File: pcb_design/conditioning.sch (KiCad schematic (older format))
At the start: 41 parts, among them U3 OPA2376AIDR, U4 LM2903DT

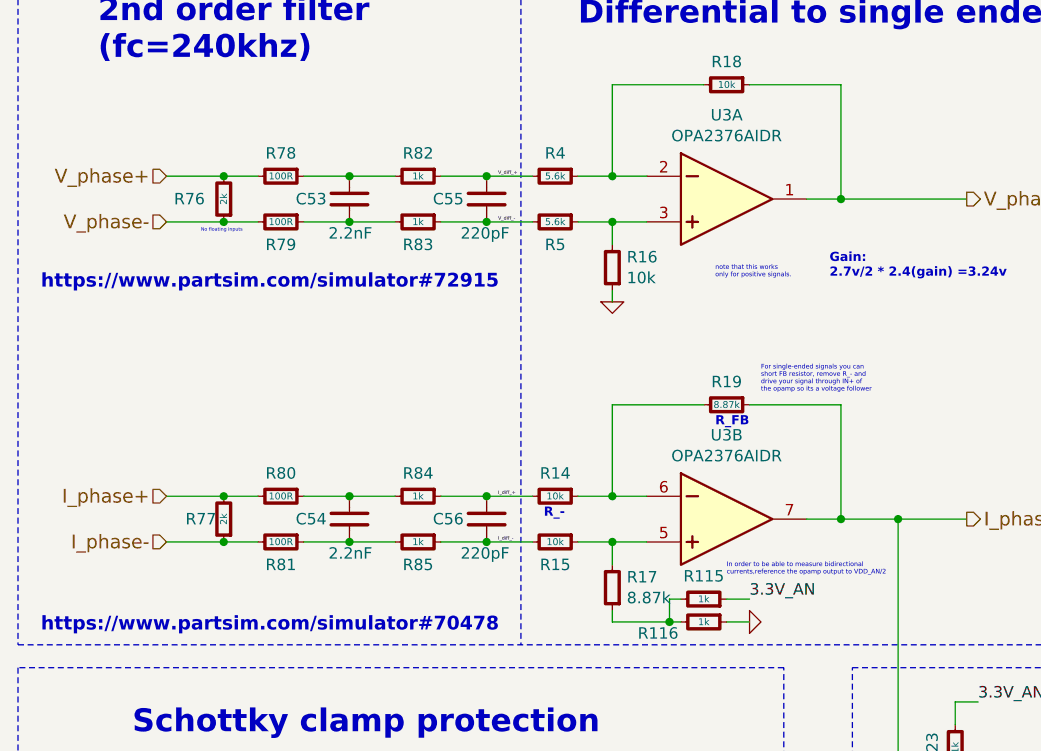
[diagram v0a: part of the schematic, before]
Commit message: Fix inverted diff signals
Signed-off-by: Marcos Chaparro <mchaparro@paltatech.com>
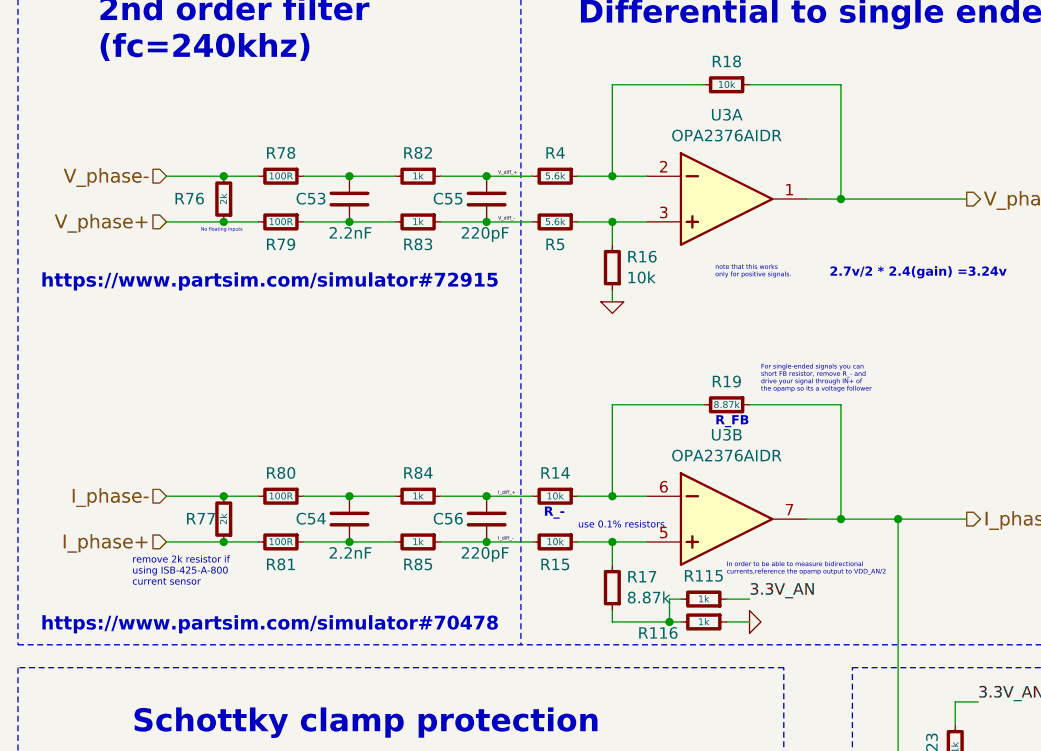
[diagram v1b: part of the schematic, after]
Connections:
- net I_phase+: now also R77.1, R81.2; no longer R77.2, R80.2
- net I_phase-: now also R77.2, R80.2; no longer R77.1, R81.2
- net V_phase+: now also R76.1, R79.2; no longer R76.2, R78.2
- net V_phase-: now also R76.2, R78.2; no longer R76.1, R79.2
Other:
- note added: "2.7v/2 * 2.4(gain) =3.24v"
- note added: "remove 2k resistor if\nusing ISB-425-A-800\ncurrent sensor"
- note added: "use 0.1% resistors"
- note removed: "Gain:\n2.7v/2 * 2.4(gain) =3.24v"
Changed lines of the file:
@@
 	1    0    0    -1
 $EndComp
+Text HLabel 3150 2650 0    60   Input ~ 0
+V_phase+
 Text HLabel 3150 2450 0    60   Input ~ 0
-V_phase+
-Text HLabel 3150 2650 0    60   Input ~ 0
 V_phase-
 Text HLabel 5000 5700 0    60   Input ~ 0
@@
 Text HLabel 3200 5250 0    60   Input ~ 0
 PWM_B
-Text HLabel 3150 3850 0    60   Input ~ 0
+Text HLabel 3150 4050 0    60   Input ~ 0
 I_phase+
 Text HLabel 6650 3950 2    60   Output ~ 0
@@
 Text HLabel 8400 5500 2    60   Output ~ 0
 ~OC_Fault
-Text HLabel 3150 4050 0    60   Input ~ 0
+Text HLabel 3150 3850 0    60   Input ~ 0
 I_phase-
 Text Notes 7100 4800 0    100  ~ 20
@@
 NoConn ~ 10300 5450
 Text Notes 6050 2900 0    40   ~ 8
-Gain:\n2.7v/2 * 2.4(gain) =3.24v
+2.7v/2 * 2.4(gain) =3.24v
 Text Notes 2600 2950 0    60   ~ 12
 https://www.partsim.com/simulator#72915
+Text Notes 4950 4000 0    30   ~ 0
+use 0.1% resistors
+Text Notes 3000 4250 0    30   ~ 0
+remove 2k resistor if\nusing ISB-425-A-800\ncurrent sensor
 $EndSCHEMATC

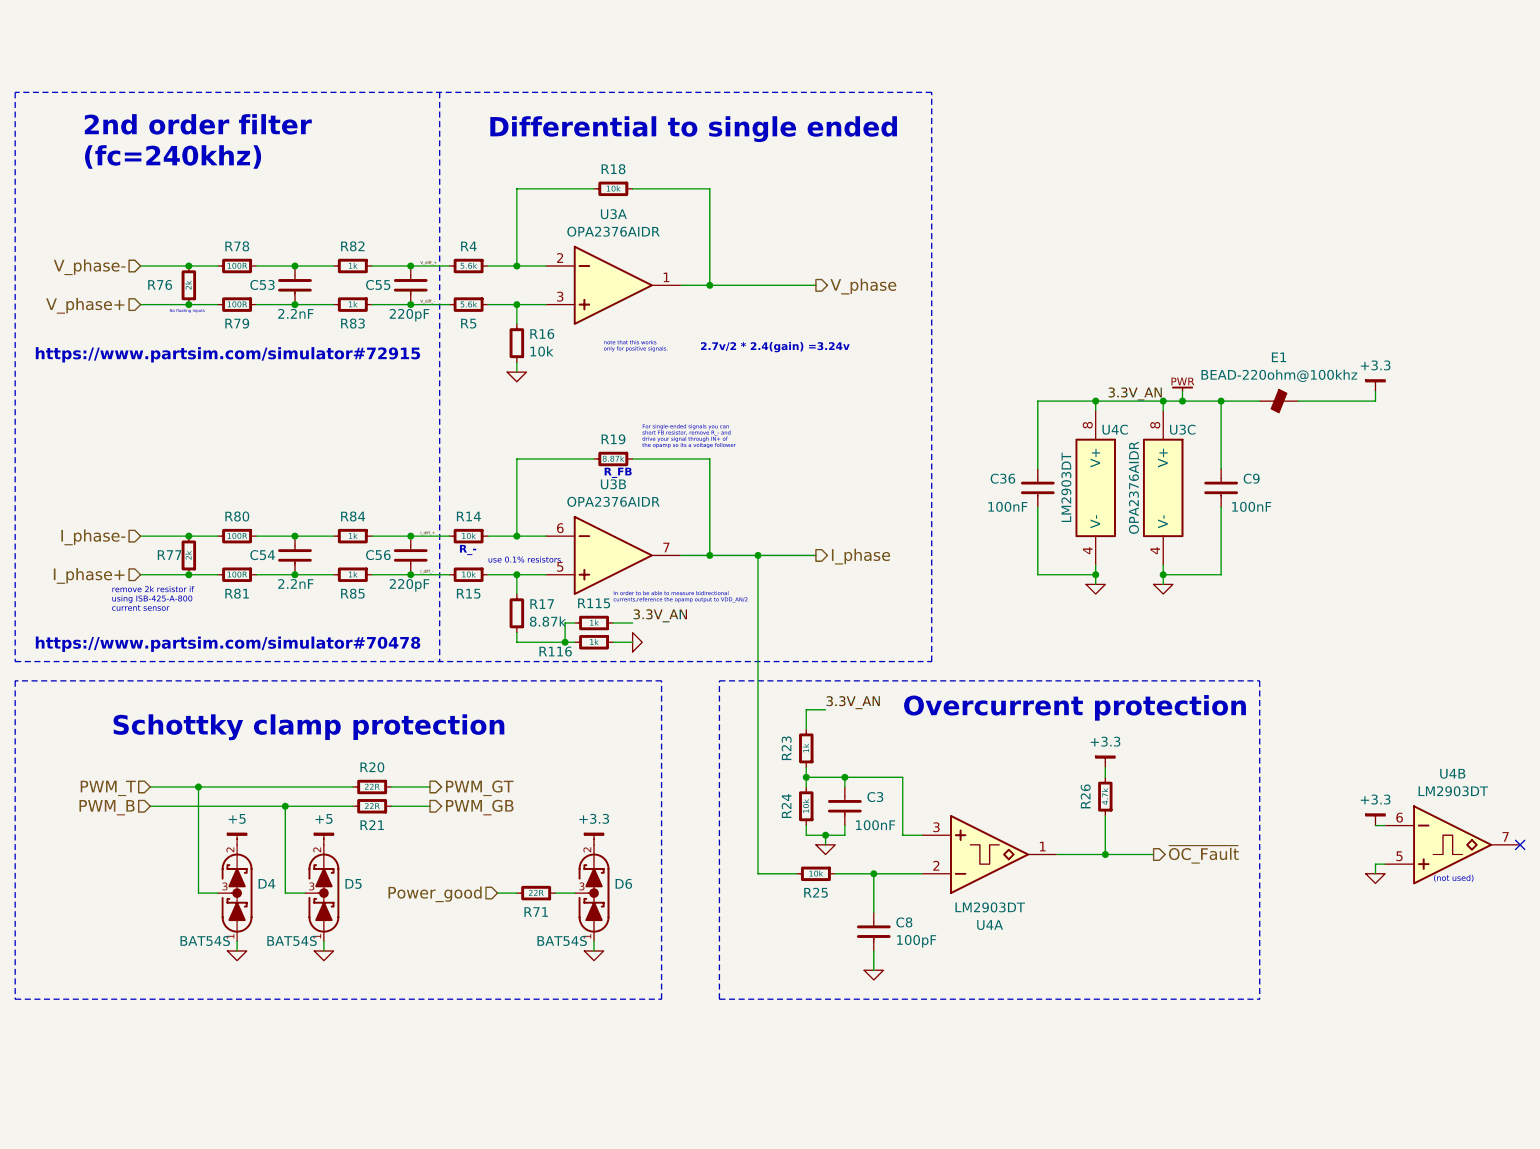
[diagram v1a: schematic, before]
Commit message: Added individual temperature sensing for each half bridge and 2 pwm gpio with low side driver
Signed-off-by: Marcos Chaparro <mchaparro@paltatech.com>
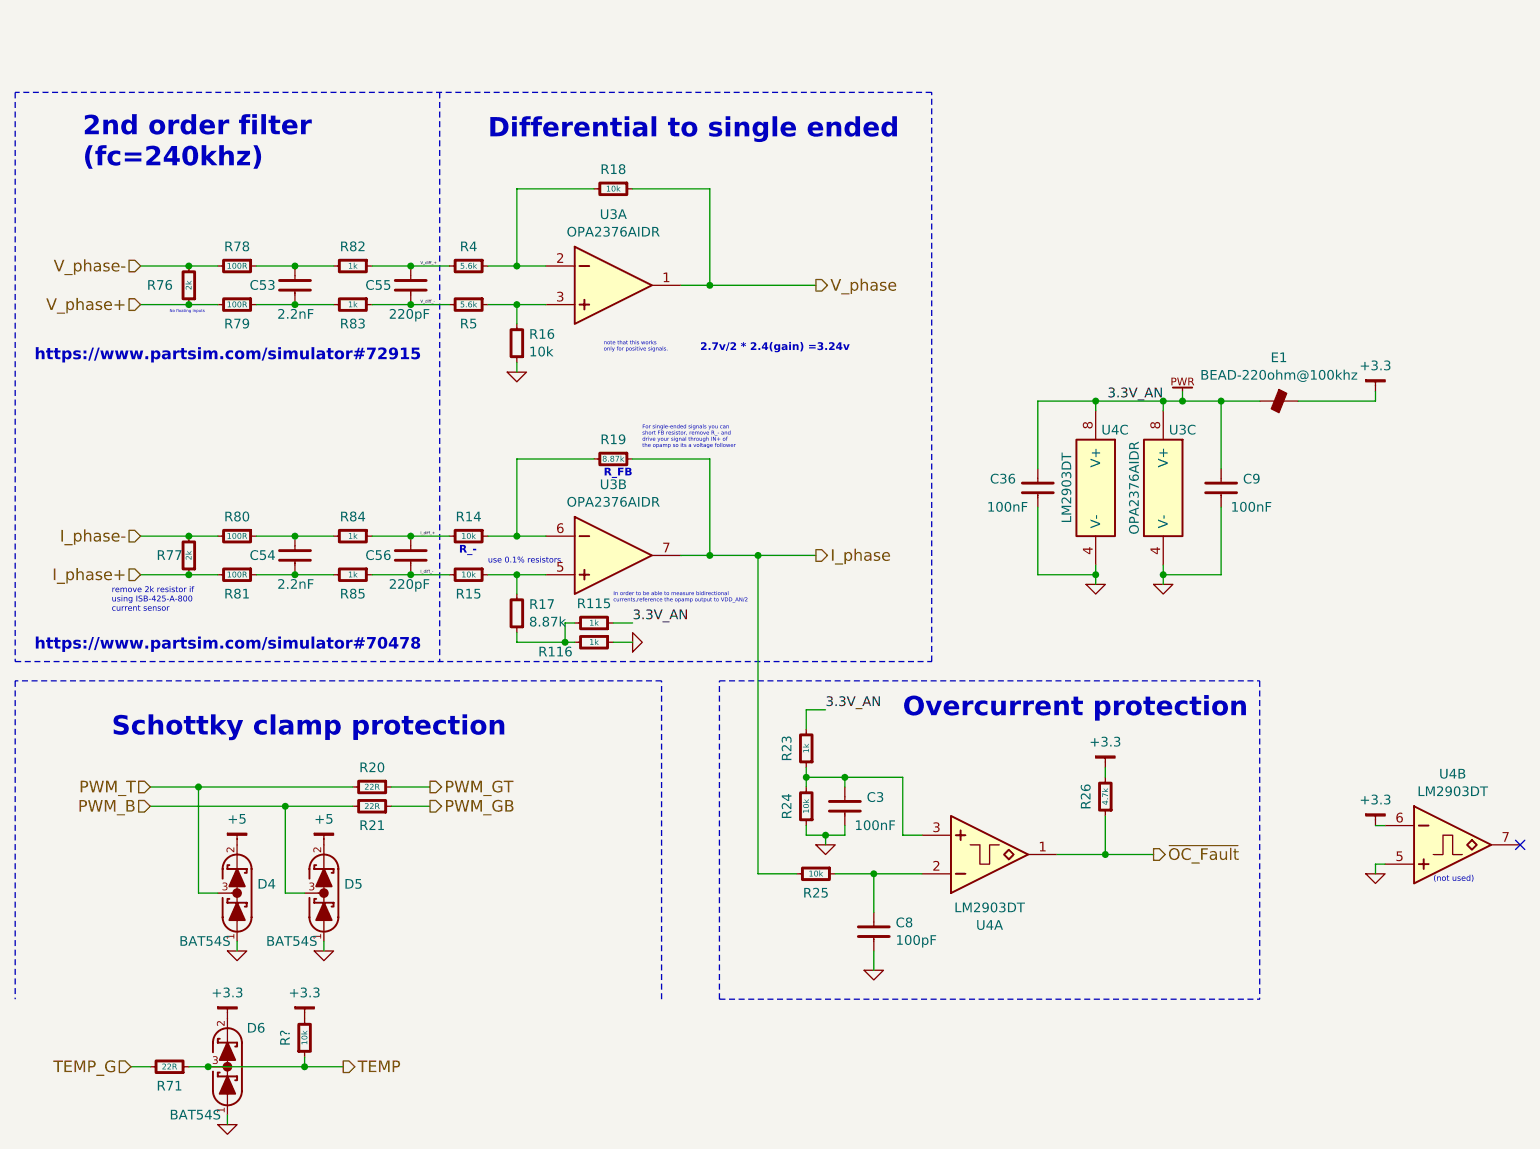
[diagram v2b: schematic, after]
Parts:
- added R?: 10k, IPC7351-Nominal:RESC1608X50, symbol R-0603
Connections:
- net +3.3: now also R?.2
- net TEMP: now reaches D6.3 (COM), R71.1
- net TEMP: now also R?.1
- net Power_good renamed TEMP_G
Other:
- moved on the sheet: D6, R71

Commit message: Fixed power supply inductor footprints in the layout
Signed-off-by: Marcos Chaparro <mchaparro@paltatech.com>
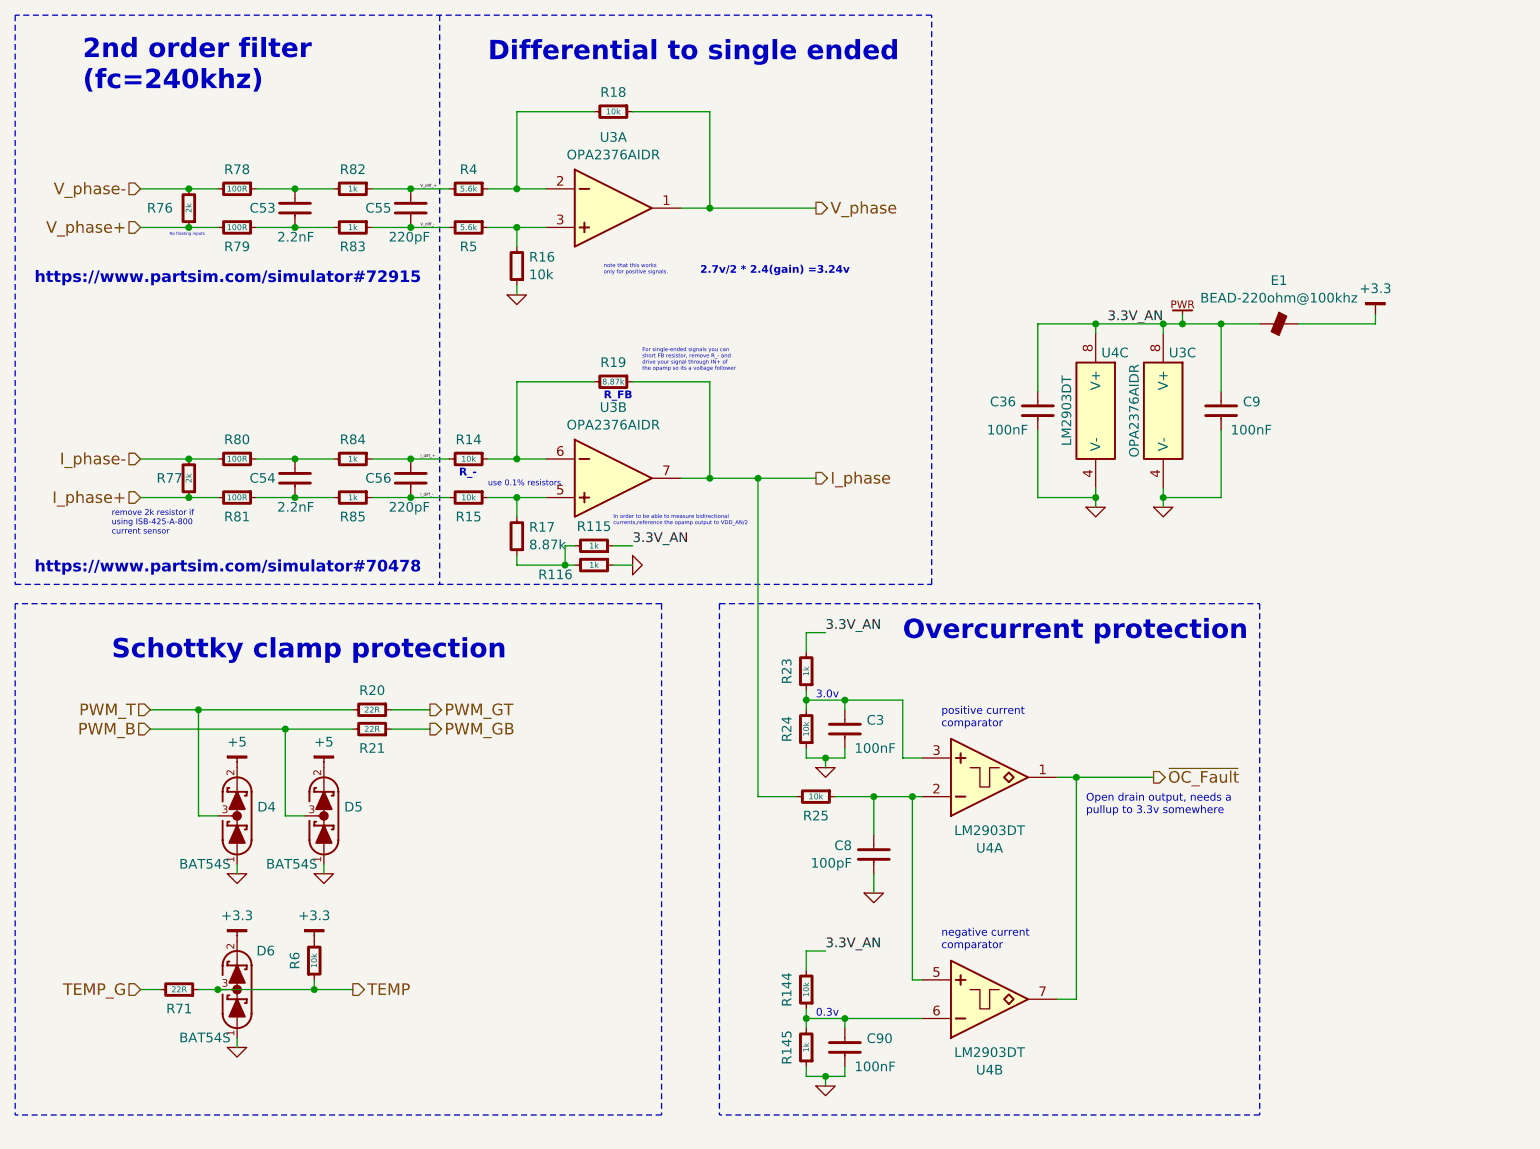
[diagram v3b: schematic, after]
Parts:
- removed R26: 4.7k, IPC7351-Nominal:RESC1608X50, symbol R-0603
- added C90: 100nF, IPC7351-Nominal:CAPC1608X55, symbol C-0603
- added R144: 10k, IPC7351-Nominal:RESC1608X50, symbol R-0603
- added R145: 1k, IPC7351-Nominal:RESC1608X50, symbol R-0603
- gave numbers to parts that had none: 1
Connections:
- net +3.3: no longer U4.6 (IN-)
- net 3.3V_AN: now also R144.2
- net GND: now also C90.2, R145.1; no longer U4.5 (IN+)
- net ~OC_Fault: now also U4.7 (OUT)
- net at C8.1, R25.1, U4.2 (IN-): now also U4.5 (IN+)
- new net: C90.1, R144.1, R145.2, U4.6 (IN-)
- no-connect marks 1 -> 0
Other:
- note added: "0.3v"
- note added: "3.0v"
- note added: "Open drain output, needs a\npullup to 3.3v somewhere"
- note added: "negative current\ncomparator"
- note added: "positive current\ncomparator"
- note removed: "(not used)"
- moved on the sheet: C3, C36, C53, C54, C55, C56, C8, C9, D4, D5, D6, E1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

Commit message: Added RC filter to FAULT line to prevent noise triggering it
Signed-off-by: Marcos Chaparro <mchaparro@paltatech.com>
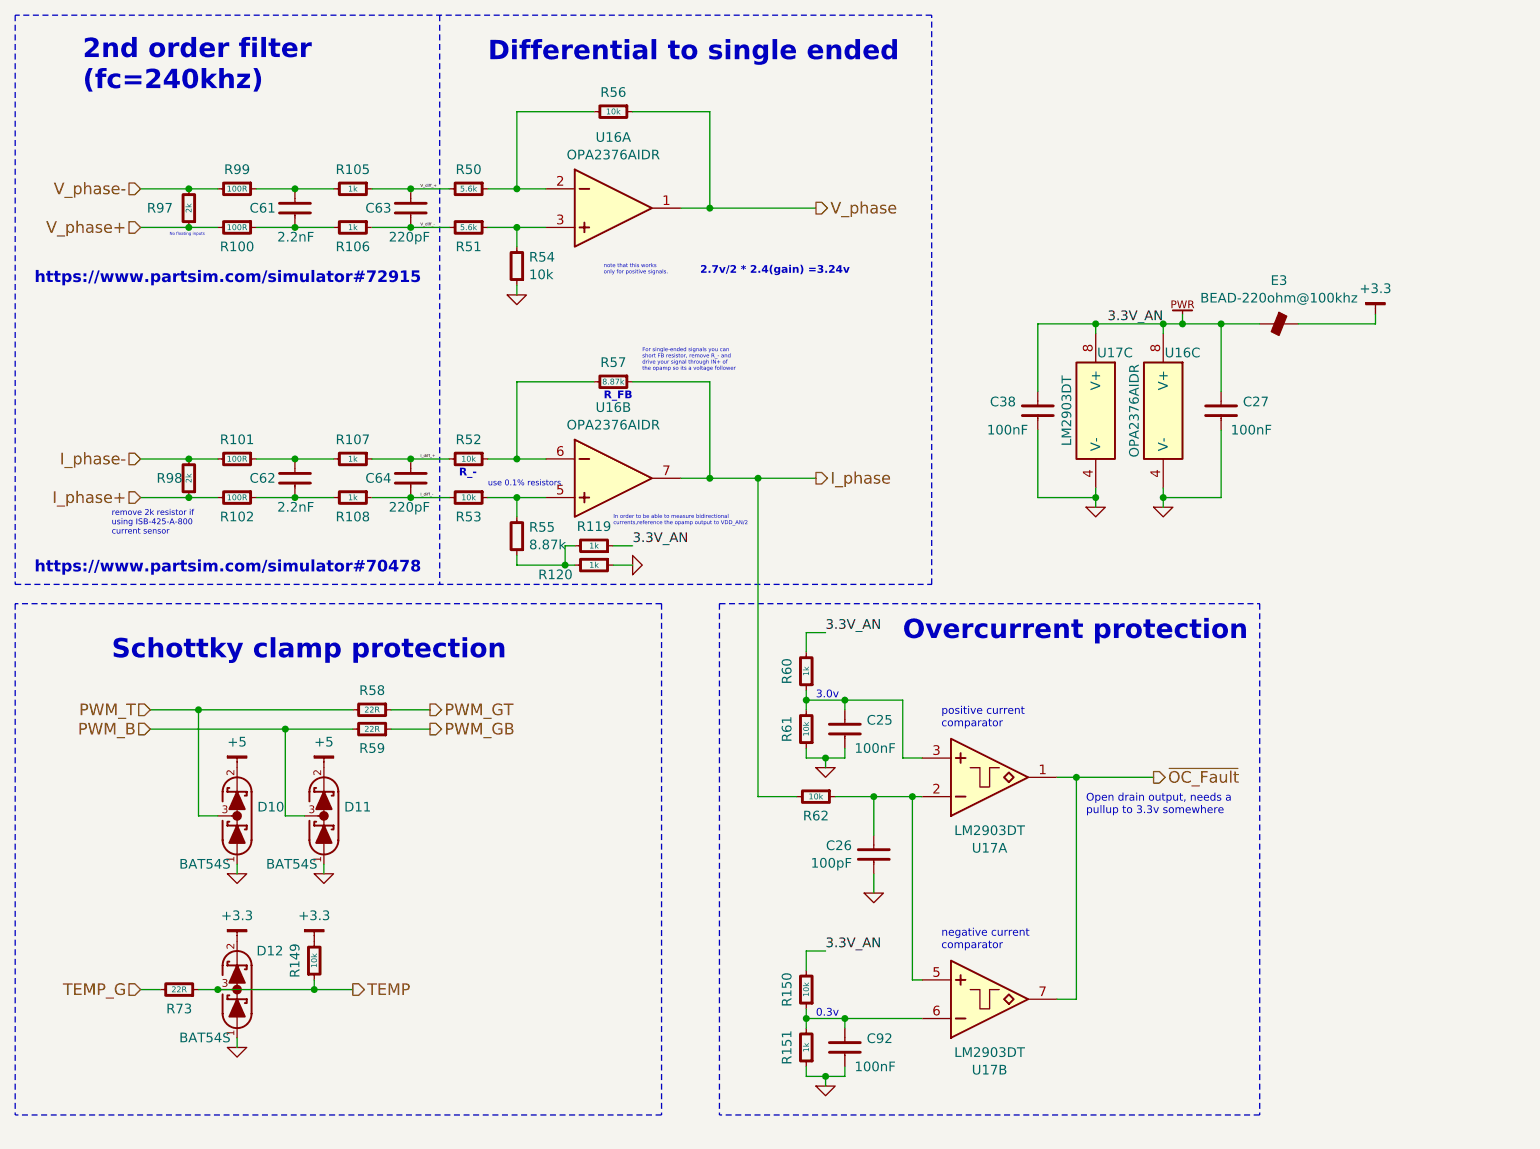
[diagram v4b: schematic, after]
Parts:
- C3, C36, C9, C90: BOM CAP MLCC 100pF C0G 50V 5% [0603] -> CAP MLCC 100nF C0G 50V 5% [0603]
- C53, C54: MPN GRM188R71H222KA01D -> (none); SPN 490-1500-1-ND -> (none)
- R14, R15: MPN RC0603FR-078K87L -> RC0603FR-0710KL; SPN 311-8.87KHRCT-ND -> 311-10.0KHRCT-ND
- R16: MFR (none) -> Yageo; MPN (none) -> RC0603FR-0710KL; SPN (none) -> 311-10.0KHRCT-ND; SPR (none) -> Digikey
- R20, R21, R71: BOM RES SMD 1k 5% [0603] -> RES SMD 22 1% [0603]; mfg# RC0603FR-0722RL -> (none)
- R6: MPN RC0603FR-0722RL -> RC0603FR-0710KL; SPN 311-22.0HRCT-ND -> 311-10.0KHRCT-ND; mfg# RC0603FR-0722RL -> (none)
